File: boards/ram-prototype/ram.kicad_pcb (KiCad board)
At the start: 4 copper layers, 200 x 84 mm, 526 parts, among them J1 PinHeader_1x24_P2.54mm_Vertic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, J2 PinHeader_1x04_P2.54mm_Vertic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, J3 PinHeader_1x14_P2.54mm_Vertic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, U1 DSBGA\-5_NumericPads, U10 DSBGA\-5_NumericPads, U100 DSBGA\-5_NumericPads, U101 DSBGA\-5_NumericPads, U102 DSBGA\-5_NumericPads, U103 DSBGA\-5_NumericPads, U104 DSBGA\-5_NumericPads, U105 DSBGA\-5_NumericPads, U106 DSBGA\-5_NumericPads, U107 DSBGA\-5_NumericPads, U108 DSBGA\-5_NumericPads, U109 DSBGA\-5_NumericPads, U11 DSBGA\-5_NumericPads, U110 DSBGA\-5_NumericPads, U111 DSBGA\-5_NumericPads, U112 DSBGA\-5_NumericPads, U113 DSBGA\-5_NumericPads, U114 DSBGA\-5_NumericPads, U115 DSBGA\-5_NumericPads, U116 DSBGA\-5_NumericPads, U117 DSBGA\-5_NumericPads, U118 DSBGA\-5_NumericPads, U119 DSBGA\-5_NumericPads, U12 DSBGA\-5_NumericPads, U120 DSBGA\-5_NumericPads, U121 DSBGA\-5_NumericPads, U122 DSBGA\-5_NumericPads, U123 DSBGA\-5_NumericPads, U124 DSBGA\-5_NumericPads, U125 DSBGA\-5_NumericPads, U126 DSBGA\-5_NumericPads, U127 DSBGA\-5_NumericPads, U128 DSBGA\-5_NumericPads, U129 DSBGA\-5_NumericPads, U13 DSBGA\-5_NumericPads, U130 DSBGA\-5_NumericPads, U131 DSBGA\-5_NumericPads, U132 DSBGA\-5_NumericPads, U133 DSBGA\-5_NumericPads, U134 DSBGA\-5_NumericPads, U135 DSBGA\-5_NumericPads, U136 DSBGA\-5_NumericPads, U137 DSBGA\-5_NumericPads, U138 DSBGA\-5_NumericPads, U139 DSBGA\-5_NumericPads, U14 DSBGA\-5_NumericPads, U140 DSBGA\-5_NumericPads, U141 DSBGA\-5_NumericPads, U142 DSBGA\-5_NumericPads, U143 DSBGA\-5_NumericPads, U144 DSBGA\-5_NumericPads, U145 DSBGA\-5_NumericPads, U146 DSBGA\-5_NumericPads, U147 DSBGA\-5_NumericPads, U148 DSBGA\-5_NumericPads, U149 DSBGA\-5_NumericPads, U15 DSBGA\-5_NumericPads, U150 DSBGA\-5_NumericPads, U151 DSBGA\-5_NumericPads, U152 DSBGA\-5_NumericPads, U153 DSBGA\-5_NumericPads, U154 DSBGA\-5_NumericPads, U155 DSBGA\-5_NumericPads, U156 DSBGA\-5_NumericPads, U157 DSBGA\-5_NumericPads, U158 DSBGA\-5_NumericPads, U159 DSBGA\-5_NumericPads, U16 DSBGA\-5_NumericPads, U160 DSBGA\-5_NumericPads, U161 DSBGA\-5_NumericPads, U162 DSBGA\-5_NumericPads, U163 DSBGA\-5_NumericPads, U164 DSBGA\-5_NumericPads, U165 DSBGA\-5_NumericPads, U166 DSBGA\-5_NumericPads, U167 DSBGA\-5_NumericPads, U168 DSBGA\-5_NumericPads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

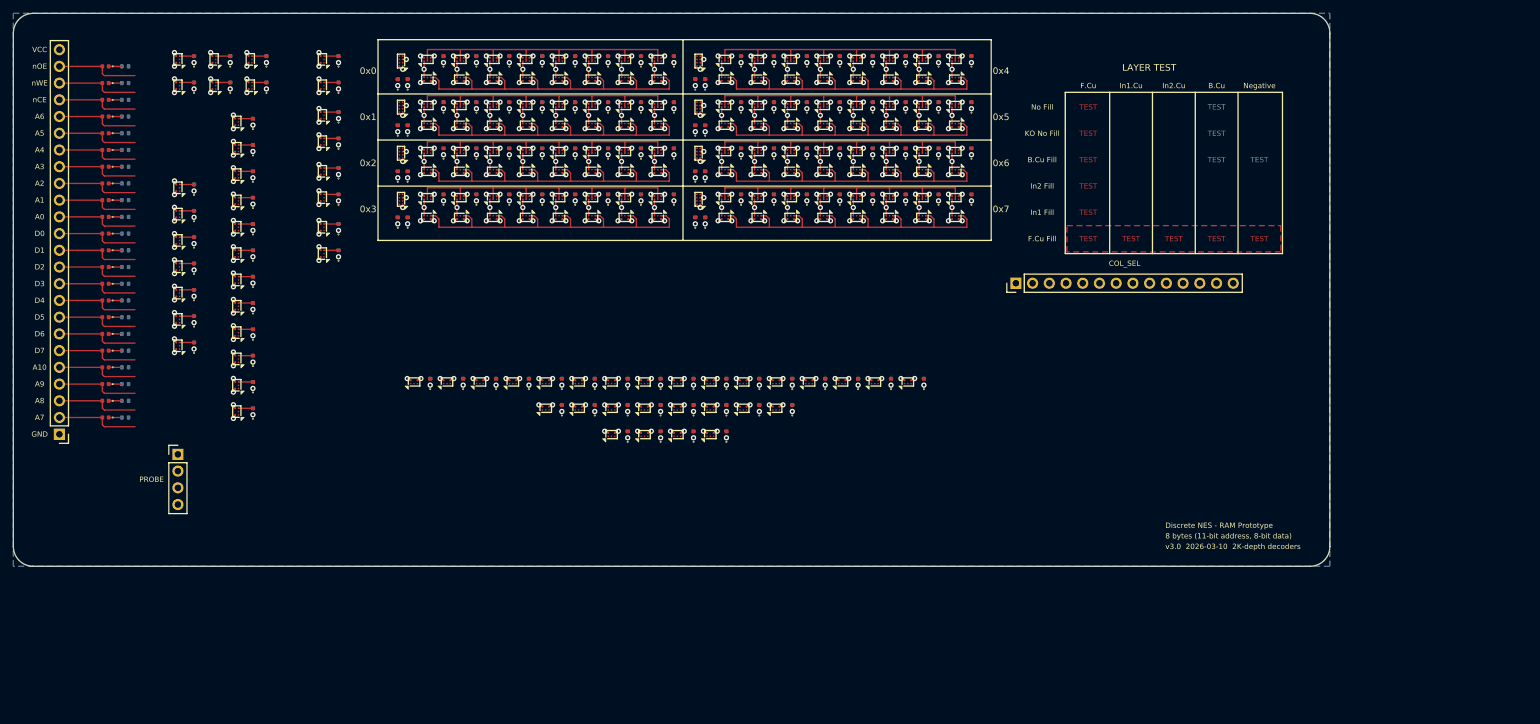
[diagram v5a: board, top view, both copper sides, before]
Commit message: Update row select to have the full complexity to test latency
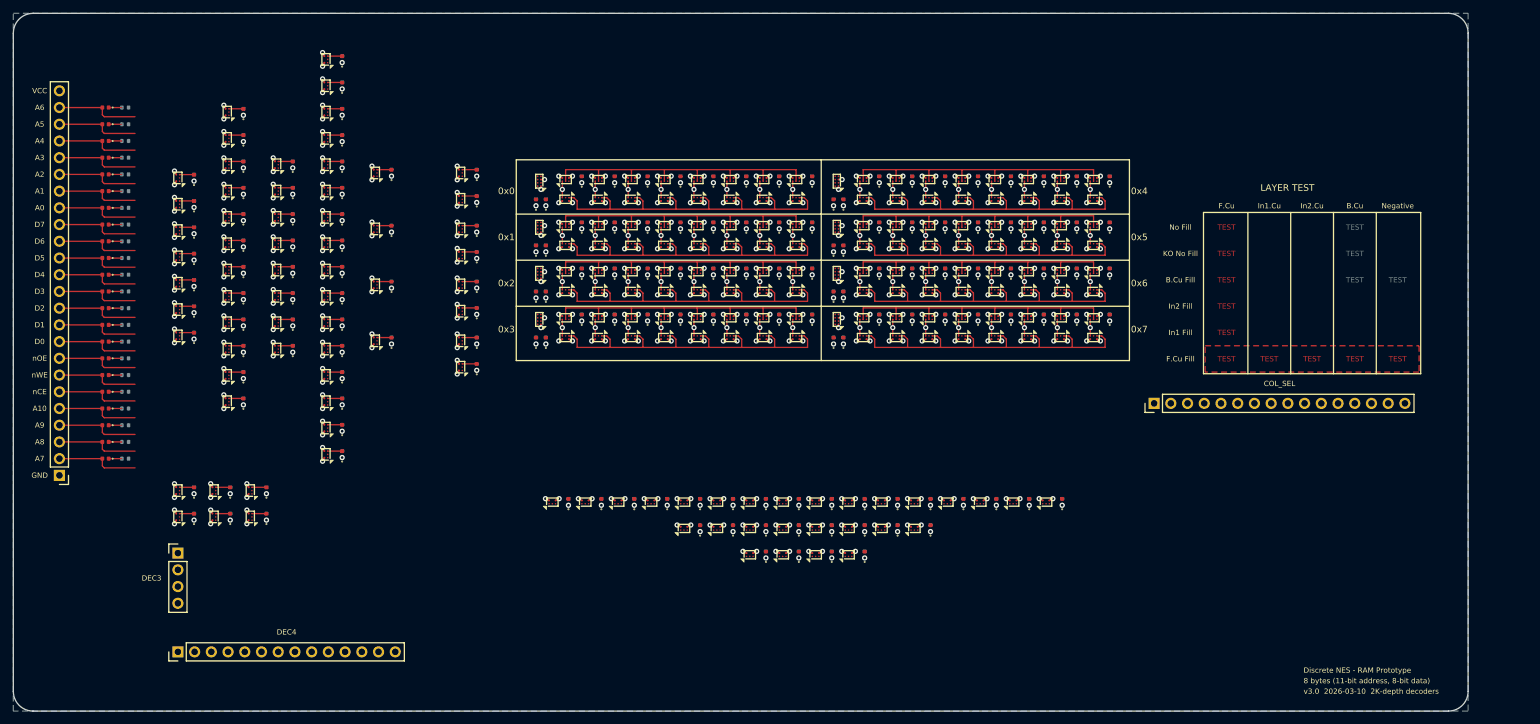
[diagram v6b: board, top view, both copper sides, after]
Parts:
- added D164: LED_0402_1005Metric, LED_SMD:LED_0402_1005Metric, F.Cu at (159.6, 38.2)
- added D165: LED_0402_1005Metric, LED_SMD:LED_0402_1005Metric, F.Cu at (159.6, 45.2)
- added D166: LED_0402_1005Metric, LED_SMD:LED_0402_1005Metric, F.Cu at (159.6, 52.2)
- added D167: LED_0402_1005Metric, LED_SMD:LED_0402_1005Metric, F.Cu at (159.6, 59.2)
- added D168: LED_0402_1005Metric, LED_SMD:LED_0402_1005Metric, F.Cu at (109.3, 38.2)
- added D169: LED_0402_1005Metric, LED_SMD:LED_0402_1005Metric, F.Cu at (109.3, 45.2)
- added D170: LED_0402_1005Metric, LED_SMD:LED_0402_1005Metric, F.Cu at (109.3, 52.2)
- added D171: LED_0402_1005Metric, LED_SMD:LED_0402_1005Metric, F.Cu at (109.3, 59.2)
- added D172: LED_0402_1005Metric, LED_SMD:LED_0402_1005Metric, F.Cu at (154.6, 38.2)
- added D173: LED_0402_1005Metric, LED_SMD:LED_0402_1005Metric, F.Cu at (154.6, 45.2)
- added D174: LED_0402_1005Metric, LED_SMD:LED_0402_1005Metric, F.Cu at (154.6, 52.2)
- added D175: LED_0402_1005Metric, LED_SMD:LED_0402_1005Metric, F.Cu at (154.6, 59.2)
- added D176: LED_0402_1005Metric, LED_SMD:LED_0402_1005Metric, F.Cu at (104.3, 38.2)
- added D177: LED_0402_1005Metric, LED_SMD:LED_0402_1005Metric, F.Cu at (104.3, 45.2)
- added D178: LED_0402_1005Metric, LED_SMD:LED_0402_1005Metric, F.Cu at (104.3, 52.2)
- added D179: LED_0402_1005Metric, LED_SMD:LED_0402_1005Metric, F.Cu at (104.3, 59.2)
- added D180: LED_0402_1005Metric, LED_SMD:LED_0402_1005Metric, F.Cu at (149.6, 38.2)
- added D181: LED_0402_1005Metric, LED_SMD:LED_0402_1005Metric, F.Cu at (149.6, 45.2)
- added D182: LED_0402_1005Metric, LED_SMD:LED_0402_1005Metric, F.Cu at (149.6, 52.2)
- added D183: LED_0402_1005Metric, LED_SMD:LED_0402_1005Metric, F.Cu at (149.6, 59.2)
- added D184: LED_0402_1005Metric, LED_SMD:LED_0402_1005Metric, F.Cu at (99.3, 38.2)
- added D185: LED_0402_1005Metric, LED_SMD:LED_0402_1005Metric, F.Cu at (99.3, 45.2)
- added D186: LED_0402_1005Metric, LED_SMD:LED_0402_1005Metric, F.Cu at (99.3, 52.2)
- added D187: LED_0402_1005Metric, LED_SMD:LED_0402_1005Metric, F.Cu at (99.3, 59.2)
- added D188: LED_0402_1005Metric, LED_SMD:LED_0402_1005Metric, F.Cu at (144.6, 38.2)
- added D189: LED_0402_1005Metric, LED_SMD:LED_0402_1005Metric, F.Cu at (144.6, 45.2)
- added D190: LED_0402_1005Metric, LED_SMD:LED_0402_1005Metric, F.Cu at (144.6, 52.2)
- added D191: LED_0402_1005Metric, LED_SMD:LED_0402_1005Metric, F.Cu at (144.6, 59.2)
- added J4: PinHeader_1x14_P2.54mm_Vertical, Connector_PinHeader_2.54mm:PinHeader_1x14_P2.54mm_Vertical, B.Cu at (38.0, 110.0)
- added R164: R_0402_1005Metric, Resistor_SMD:R_0402_1005Metric, B.Cu at (159.6, 38.2)
- added R165: R_0402_1005Metric, Resistor_SMD:R_0402_1005Metric, B.Cu at (159.6, 45.2)
- added R166: R_0402_1005Metric, Resistor_SMD:R_0402_1005Metric, B.Cu at (159.6, 52.2)
- added R167: R_0402_1005Metric, Resistor_SMD:R_0402_1005Metric, B.Cu at (159.6, 59.2)
- added R168: R_0402_1005Metric, Resistor_SMD:R_0402_1005Metric, B.Cu at (109.3, 38.2)
- added R169: R_0402_1005Metric, Resistor_SMD:R_0402_1005Metric, B.Cu at (109.3, 45.2)
- added R170: R_0402_1005Metric, Resistor_SMD:R_0402_1005Metric, B.Cu at (109.3, 52.2)
- added R171: R_0402_1005Metric, Resistor_SMD:R_0402_1005Metric, B.Cu at (109.3, 59.2)
- added R172: R_0402_1005Metric, Resistor_SMD:R_0402_1005Metric, B.Cu at (154.6, 38.2)
- added R173: R_0402_1005Metric, Resistor_SMD:R_0402_1005Metric, B.Cu at (154.6, 45.2)
- added R174: R_0402_1005Metric, Resistor_SMD:R_0402_1005Metric, B.Cu at (154.6, 52.2)
- added R175: R_0402_1005Metric, Resistor_SMD:R_0402_1005Metric, B.Cu at (154.6, 59.2)
- added R176: R_0402_1005Metric, Resistor_SMD:R_0402_1005Metric, B.Cu at (104.3, 38.2)
- added R177: R_0402_1005Metric, Resistor_SMD:R_0402_1005Metric, B.Cu at (104.3, 45.2)
- added R178: R_0402_1005Metric, Resistor_SMD:R_0402_1005Metric, B.Cu at (104.3, 52.2)
- added R179: R_0402_1005Metric, Resistor_SMD:R_0402_1005Metric, B.Cu at (104.3, 59.2)
- added R180: R_0402_1005Metric, Resistor_SMD:R_0402_1005Metric, B.Cu at (149.6, 38.2)
- added R181: R_0402_1005Metric, Resistor_SMD:R_0402_1005Metric, B.Cu at (149.6, 45.2)
- added R182: R_0402_1005Metric, Resistor_SMD:R_0402_1005Metric, B.Cu at (149.6, 52.2)
- added R183: R_0402_1005Metric, Resistor_SMD:R_0402_1005Metric, B.Cu at (149.6, 59.2)
- added R184: R_0402_1005Metric, Resistor_SMD:R_0402_1005Metric, B.Cu at (99.3, 38.2)
- added R185: R_0402_1005Metric, Resistor_SMD:R_0402_1005Metric, B.Cu at (99.3, 45.2)
- added R186: R_0402_1005Metric, Resistor_SMD:R_0402_1005Metric, B.Cu at (99.3, 52.2)
- added R187: R_0402_1005Metric, Resistor_SMD:R_0402_1005Metric, B.Cu at (99.3, 59.2)
- added R188: R_0402_1005Metric, Resistor_SMD:R_0402_1005Metric, B.Cu at (144.6, 38.2)
- added R189: R_0402_1005Metric, Resistor_SMD:R_0402_1005Metric, B.Cu at (144.6, 45.2)
- added R190: R_0402_1005Metric, Resistor_SMD:R_0402_1005Metric, B.Cu at (144.6, 52.2)
- added R191: R_0402_1005Metric, Resistor_SMD:R_0402_1005Metric, B.Cu at (144.6, 59.2)
- added U198: DSBGA\-5_NumericPads, DSBGA_Packages:DSBGA-5_NumericPads, F.Cu at (147.1, 38.2)
- added U199: DSBGA\-5_NumericPads, DSBGA_Packages:DSBGA-5_NumericPads, F.Cu at (147.1, 45.2)
- added U200: DSBGA\-5_NumericPads, DSBGA_Packages:DSBGA-5_NumericPads, F.Cu at (147.1, 52.2)
- added U201: DSBGA\-5_NumericPads, DSBGA_Packages:DSBGA-5_NumericPads, F.Cu at (147.1, 59.2)
- added U202: DSBGA\-5_NumericPads, DSBGA_Packages:DSBGA-5_NumericPads, F.Cu at (101.9, 41.2)
- added U203: DSBGA\-5_NumericPads, DSBGA_Packages:DSBGA-5_NumericPads, F.Cu at (101.9, 48.2)
- added U204: DSBGA\-5_NumericPads, DSBGA_Packages:DSBGA-5_NumericPads, F.Cu at (101.9, 55.2)
- added U205: DSBGA\-5_NumericPads, DSBGA_Packages:DSBGA-5_NumericPads, F.Cu at (101.9, 62.2)
- added U206: DSBGA\-5_NumericPads, DSBGA_Packages:DSBGA-5_NumericPads, F.Cu at (147.1, 41.2)
- added U207: DSBGA\-5_NumericPads, DSBGA_Packages:DSBGA-5_NumericPads, F.Cu at (147.1, 48.2)
- added U208: DSBGA\-5_NumericPads, DSBGA_Packages:DSBGA-5_NumericPads, F.Cu at (147.1, 55.2)
- added U209: DSBGA\-5_NumericPads, DSBGA_Packages:DSBGA-5_NumericPads, F.Cu at (147.1, 62.2)
- added U210: DSBGA\-5_NumericPads, DSBGA_Packages:DSBGA-5_NumericPads, F.Cu at (96.9, 38.2)
- added U211: DSBGA\-5_NumericPads, DSBGA_Packages:DSBGA-5_NumericPads, F.Cu at (96.9, 45.2)
- added U212: DSBGA\-5_NumericPads, DSBGA_Packages:DSBGA-5_NumericPads, F.Cu at (96.9, 52.2)
- added U213: DSBGA\-5_NumericPads, DSBGA_Packages:DSBGA-5_NumericPads, F.Cu at (96.9, 59.2)
- added U214: DSBGA\-5_NumericPads, DSBGA_Packages:DSBGA-5_NumericPads, F.Cu at (142.1, 38.2)
- added U215: DSBGA\-5_NumericPads, DSBGA_Packages:DSBGA-5_NumericPads, F.Cu at (142.1, 45.2)
- added U216: DSBGA\-5_NumericPads, DSBGA_Packages:DSBGA-5_NumericPads, F.Cu at (142.1, 52.2)
- added U217: DSBGA\-5_NumericPads, DSBGA_Packages:DSBGA-5_NumericPads, F.Cu at (142.1, 59.2)
- added U218: DSBGA\-5_NumericPads, DSBGA_Packages:DSBGA-5_NumericPads, F.Cu at (96.9, 41.2)
- added U219: DSBGA\-5_NumericPads, DSBGA_Packages:DSBGA-5_NumericPads, F.Cu at (96.9, 48.2)
- added U220: DSBGA\-5_NumericPads, DSBGA_Packages:DSBGA-5_NumericPads, F.Cu at (96.9, 55.2)
- added U221: DSBGA\-5_NumericPads, DSBGA_Packages:DSBGA-5_NumericPads, F.Cu at (96.9, 62.2)
- added U222: DSBGA\-5_NumericPads, DSBGA_Packages:DSBGA-5_NumericPads, F.Cu at (142.1, 41.2)
- added U223: DSBGA\-5_NumericPads, DSBGA_Packages:DSBGA-5_NumericPads, F.Cu at (142.1, 48.2)
- added U224: DSBGA\-5_NumericPads, DSBGA_Packages:DSBGA-5_NumericPads, F.Cu at (142.1, 55.2)
- added U225: DSBGA\-5_NumericPads, DSBGA_Packages:DSBGA-5_NumericPads, F.Cu at (142.1, 62.2)
- J3: value PinHeader_1x14_P2.54mm_Vertical -> PinHeader_1x16_P2.54mm_Vertical; footprint Connector_PinHeader_2.54mm:PinHeader_1x14_P2.54mm_Vertical -> Connector_PinHeader_2.54mm:PinHeader_1x16_P2.54mm_Vertical
- U62, U63, U64, U65, U66, U67, U68, U69: value DSBGA\-8_NumericPads -> DSBGA\-5_NumericPads; footprint DSBGA_Packages:DSBGA-8_NumericPads -> DSBGA_Packages:DSBGA-5_NumericPads
- U90, U91, U92, U93, U94, U95, U96, U97: value DSBGA\-5_NumericPads -> DSBGA\-8_NumericPads; footprint DSBGA_Packages:DSBGA-5_NumericPads -> DSBGA_Packages:DSBGA-8_NumericPads
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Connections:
- D1 pad 2: /Control Logic/nOE -> /Address Decoder/A6
- D10 pad 2: /Address Decoder/A0 -> /D5
- D100 pad 2: Net-(D100-A) -> /WRITE_EN_ROW_2
- D101 pad 2: Net-(D101-A) -> /WRITE_EN_ROW_3
- D102 pad 2: Net-(D102-A) -> /READ_EN_ROW_0
- D103 pad 2: Net-(D103-A) -> /READ_EN_ROW_1
- D104 pad 2: Net-(D104-A) -> /READ_EN_ROW_2
- D105 pad 2: Net-(D105-A) -> /READ_EN_ROW_3
- D11 pad 2: /D0 -> /D4
- D110 pad 2: Net-(D110-A) -> /WRITE_ACTIVE
- D111 pad 2: Net-(D111-A) -> /READ_EN
- D12 pad 2: /D1 -> /D3
- D14 pad 2: /D3 -> /D1
- D15 pad 2: /D4 -> /D0
- D16 pad 2: /D5 -> /nOE
- D17 pad 2: /D6 -> /nWE
- D18 pad 2: /D7 -> /nCE
- D2 pad 2: /Control Logic/nWE -> /Address Decoder/A5
- D23 pad 2: Net-(D23-A) -> /Address Decoder/nA0
- D24 pad 2: Net-(D24-A) -> /Address Decoder/nA1
- D25 pad 2: Net-(D25-A) -> /Address Decoder/nA2
- D26 pad 2: Net-(D26-A) -> /Address Decoder/nA3
- D27 pad 2: Net-(D27-A) -> /Address Decoder/nA4
- D28 pad 2: Net-(D28-A) -> /Address Decoder/nA5
- D29 pad 2: Net-(D29-A) -> /Address Decoder/nA6
- D3 pad 2: /Control Logic/nCE -> /Address Decoder/A4
- D30 pad 2: /RS1 -> /Address Decoder/G0
- D31 pad 2: /RS2 -> /Address Decoder/G1
- D32 pad 2: /RS3 -> /Address Decoder/G2
- D33 pad 2: /RS4 -> /Address Decoder/G3
- D34 pad 2: Net-(D34-A) -> /Address Decoder/DEC3_0
- D35 pad 2: Net-(D35-A) -> /Address Decoder/DEC3_1
- D36 pad 2: Net-(D36-A) -> /Address Decoder/DEC3_2
- D37 pad 2: Net-(D37-A) -> /Address Decoder/DEC3_3
- D38 pad 2: /Address Decoder/ROW_SEL_0 -> /DEC3_4
- D39 pad 2: /Address Decoder/ROW_SEL_1 -> /DEC3_5
- D4 pad 2: /Address Decoder/A6 -> /Address Decoder/A3
- D40 pad 2: /Address Decoder/ROW_SEL_2 -> /DEC3_6
- D41 pad 2: /Address Decoder/ROW_SEL_3 -> /DEC3_7
- D42 pad 2: Net-(D42-A) -> /Address Decoder/HA0
- D43 pad 2: Net-(D43-A) -> /Address Decoder/HA1
- D44 pad 2: Net-(D44-A) -> /Address Decoder/HA2
- D45 pad 2: Net-(D45-A) -> /Address Decoder/HA3
- D46 pad 2: /Column Select/GA0 -> /Address Decoder/HB0
- D47 pad 2: /Column Select/GA1 -> /Address Decoder/HB1
- D48 pad 2: /Column Select/GA2 -> /Address Decoder/HB2
- D49 pad 2: /Column Select/GA3 -> /Address Decoder/HB3
- D5 pad 2: /Address Decoder/A5 -> /Address Decoder/A2
- D50 pad 2: /Column Select/GB0 -> /Address Decoder/DEC4_0
- D51 pad 2: /Column Select/GB1 -> /DEC4_1
- D52 pad 2: /Column Select/GB2 -> /DEC4_2
- D53 pad 2: /Column Select/GB3 -> /DEC4_3
- D54 pad 2: /COL_SEL_0 -> /DEC4_4
- D55 pad 2: /COL_SEL_1 -> /DEC4_5
- D56 pad 2: /COL_SEL_2 -> /DEC4_6
- D57 pad 2: /COL_SEL_3 -> /DEC4_7
- D58 pad 2: /COL_SEL_4 -> /DEC4_8
- D59 pad 2: /COL_SEL_5 -> /DEC4_9
- D6 pad 2: /Address Decoder/A4 -> /Address Decoder/A1
- D60 pad 2: /COL_SEL_6 -> /DEC4_10
- D61 pad 2: /COL_SEL_7 -> /DEC4_11
- D62 pad 2: /COL_SEL_8 -> /DEC4_12
- D63 pad 2: /COL_SEL_9 -> /DEC4_13
- D64 pad 2: /COL_SEL_10 -> /DEC4_14
- D65 pad 2: /COL_SEL_11 -> /DEC4_15
- D66 pad 2: /COL_SEL_12 -> /Address Decoder/ROW_SEL_0
- D67 pad 2: /COL_SEL_13 -> /Address Decoder/ROW_SEL_1
- D68 pad 2: /COL_SEL_14 -> /Address Decoder/ROW_SEL_2
- D69 pad 2: /COL_SEL_15 -> /Address Decoder/ROW_SEL_3
- D7 pad 2: /Address Decoder/A3 -> /Address Decoder/A0
- D74 pad 2: /WRITE_ACTIVE -> /Column Select/GA0
- D75 pad 2: /READ_EN -> /Column Select/GA1
- D76 pad 2: /WRITE_EN_ROW_0 -> /Column Select/GA2
- D77 pad 2: /WRITE_EN_ROW_1 -> /Column Select/GA3
- D78 pad 2: /WRITE_EN_ROW_2 -> /Column Select/GB0
- D79 pad 2: /WRITE_EN_ROW_3 -> /Column Select/GB1
- D8 pad 2: /Address Decoder/A2 -> /D7
- D80 pad 2: /READ_EN_ROW_0 -> /Column Select/GB2
- D81 pad 2: /READ_EN_ROW_1 -> /Column Select/GB3
- D82 pad 2: /READ_EN_ROW_2 -> /COL_SEL_0
- D83 pad 2: /READ_EN_ROW_3 -> /COL_SEL_1
- D84 pad 2: Net-(D84-A) -> /COL_SEL_2
- D85 pad 2: Net-(D85-A) -> /COL_SEL_3
- D86 pad 2: Net-(D86-A) -> /COL_SEL_4
- D87 pad 2: Net-(D87-A) -> /COL_SEL_5
- D88 pad 2: Net-(D88-A) -> /COL_SEL_6
- D89 pad 2: Net-(D89-A) -> /COL_SEL_7
- D9 pad 2: /Address Decoder/A1 -> /D6
- D90 pad 2: Net-(D90-A) -> /COL_SEL_8
- D91 pad 2: Net-(D91-A) -> /COL_SEL_9
- D92 pad 2: Net-(D92-A) -> /COL_SEL_10
- D93 pad 2: Net-(D93-A) -> /COL_SEL_11
- D94 pad 2: Net-(D94-A) -> /COL_SEL_12
- D95 pad 2: Net-(D95-A) -> /COL_SEL_13
- D96 pad 2: Net-(D96-A) -> /COL_SEL_14
- D97 pad 2: Net-(D97-A) -> /COL_SEL_15
- D98 pad 2: Net-(D98-A) -> /WRITE_EN_ROW_0
- D99 pad 2: Net-(D99-A) -> /WRITE_EN_ROW_1
- J1 pad 10: /D3 -> /D1
- J1 pad 12: /D1 -> /D3
- J1 pad 13: /D0 -> /D4
- J1 pad 14: /Address Decoder/A0 -> /D5
- J1 pad 15: /Address Decoder/A1 -> /D6
- J1 pad 16: /Address Decoder/A2 -> /D7
- J1 pad 17: /Address Decoder/A3 -> /Address Decoder/A0
- J1 pad 18: /Address Decoder/A4 -> /Address Decoder/A1
- J1 pad 19: /Address Decoder/A5 -> /Address Decoder/A2
- J1 pad 20: /Address Decoder/A6 -> /Address Decoder/A3
- J1 pad 21: /Control Logic/nCE -> /Address Decoder/A4
- J1 pad 22: /Control Logic/nWE -> /Address Decoder/A5
- J1 pad 23: /Control Logic/nOE -> /Address Decoder/A6
- J1 pad 6: /D7 -> /nCE
- J1 pad 7: /D6 -> /nWE
- J1 pad 8: /D5 -> /nOE
- J1 pad 9: /D4 -> /D0
- J2 pad 1: /RS1 -> /DEC3_4
- J2 pad 2: /RS2 -> /DEC3_5
- J2 pad 3: /RS3 -> /DEC3_6
- J2 pad 4: /RS4 -> /DEC3_7
- J3 pad 1: /COL_SEL_2 -> /DEC4_1
- J3 pad 10: /COL_SEL_11 -> /DEC4_10
- J3 pad 11: /COL_SEL_12 -> /DEC4_11
- J3 pad 12: /COL_SEL_13 -> /DEC4_12
- J3 pad 13: /COL_SEL_14 -> /DEC4_13
- J3 pad 14: /COL_SEL_15 -> /DEC4_14
- J3 pad 2: /COL_SEL_3 -> /DEC4_2
- J3 pad 3: /COL_SEL_4 -> /DEC4_3
- J3 pad 4: /COL_SEL_5 -> /DEC4_4
- J3 pad 5: /COL_SEL_6 -> /DEC4_5
- J3 pad 6: /COL_SEL_7 -> /DEC4_6
- J3 pad 7: /COL_SEL_8 -> /DEC4_7
- J3 pad 8: /COL_SEL_9 -> /DEC4_8
- J3 pad 9: /COL_SEL_10 -> /DEC4_9
- U1 pad 4: Net-(D23-A) -> /Address Decoder/nA0
- U10 pad 1: /RS1 -> /Address Decoder/A2
- U10 pad 2: /RS2 -> /Address Decoder/nA1
- U10 pad 4: /RS3 -> /Address Decoder/G2
- U100 pad 1: Net-(D98-A) -> /D0
- U100 pad 4: /D1 -> Net-(D130-A)
- U101 pad 1: Net-(D99-A) -> /D0
- U101 pad 4: /D1 -> Net-(D131-A)
- U102 pad 1: /D2 -> /D0
- U102 pad 2: Net-(D84-A) -> Net-(D116-A)
- U102 pad 4: Net-(D116-A) -> Net-(D132-A)
- U103 pad 1: /D2 -> /D0
- U103 pad 2: Net-(D85-A) -> Net-(D117-A)
- U103 pad 4: Net-(D117-A) -> Net-(D133-A)
- U104 pad 1: /D2 -> /D0
- U104 pad 2: Net-(D86-A) -> Net-(D118-A)
- U104 pad 4: Net-(D118-A) -> Net-(D134-A)
- U105 pad 1: /D2 -> /D0
- U105 pad 2: Net-(D87-A) -> Net-(D119-A)
- U105 pad 4: Net-(D119-A) -> Net-(D135-A)
- U106 pad 1: /D2 -> Net-(D120-A)
- U106 pad 2: Net-(D88-A) -> Net-(D128-A)
- U106 pad 4: Net-(D120-A) -> /D0
- U107 pad 1: /D2 -> Net-(D121-A)
- U107 pad 2: Net-(D89-A) -> Net-(D129-A)
- U107 pad 4: Net-(D121-A) -> /D0
- U108 pad 1: /D2 -> Net-(D122-A)
- U108 pad 2: Net-(D90-A) -> Net-(D130-A)
- U108 pad 4: Net-(D122-A) -> /D0
- U109 pad 1: /D2 -> Net-(D123-A)
- U109 pad 2: Net-(D91-A) -> Net-(D131-A)
- U109 pad 4: Net-(D123-A) -> /D0
- U11 pad 1: /RS3 -> /Address Decoder/A2
- U11 pad 2: Net-(D29-A) -> /Address Decoder/A1
- U11 pad 4: /RS4 -> /Address Decoder/G3
- U110 pad 1: Net-(D92-A) -> Net-(D124-A)
- U110 pad 2: Net-(D116-A) -> Net-(D132-A)
- U110 pad 4: /D2 -> /D0
- U111 pad 1: Net-(D93-A) -> Net-(D125-A)
- U111 pad 2: Net-(D117-A) -> Net-(D133-A)
- U111 pad 4: /D2 -> /D0
- U112 pad 1: Net-(D94-A) -> Net-(D126-A)
- U112 pad 2: Net-(D118-A) -> Net-(D134-A)
- U112 pad 4: /D2 -> /D0
- U113 pad 1: Net-(D95-A) -> Net-(D127-A)
- U113 pad 2: Net-(D119-A) -> Net-(D135-A)
- U113 pad 4: /D2 -> /D0
- U114 pad 1: Net-(D96-A) -> /D1
- U114 pad 2: Net-(D120-A) -> Net-(D112-A)
- U114 pad 4: /D2 -> Net-(D136-A)
- U115 pad 1: Net-(D97-A) -> /D1
- U115 pad 2: Net-(D121-A) -> Net-(D113-A)
- U115 pad 4: /D2 -> Net-(D137-A)
- U116 pad 1: Net-(D98-A) -> /D1
- U116 pad 2: Net-(D122-A) -> Net-(D114-A)
- U116 pad 4: /D2 -> Net-(D138-A)
- U117 pad 1: Net-(D99-A) -> /D1
- U117 pad 2: Net-(D123-A) -> Net-(D115-A)
- U117 pad 4: /D2 -> Net-(D139-A)
- U118 pad 1: /D3 -> /D1
- U118 pad 2: Net-(D84-A) -> Net-(D116-A)
- U118 pad 4: Net-(D124-A) -> Net-(D140-A)
- U119 pad 1: /D3 -> /D1
- U119 pad 2: Net-(D85-A) -> Net-(D117-A)
- U119 pad 4: Net-(D125-A) -> Net-(D141-A)
- U12 pad 1: Net-(D24-A) -> /Address Decoder/G0
- U12 pad 2: Net-(D23-A) -> /Address Decoder/nA0
- U12 pad 4: Net-(D34-A) -> /Address Decoder/DEC3_0
- U120 pad 1: /D3 -> /D1
- U120 pad 2: Net-(D86-A) -> Net-(D118-A)
- U120 pad 4: Net-(D126-A) -> Net-(D142-A)
- U121 pad 1: /D3 -> /D1
- U121 pad 2: Net-(D87-A) -> Net-(D119-A)
- U121 pad 4: Net-(D127-A) -> Net-(D143-A)
- U122 pad 1: /D3 -> Net-(D120-A)
- U122 pad 2: Net-(D88-A) -> Net-(D136-A)
- U122 pad 4: Net-(D128-A) -> /D1
- U123 pad 1: /D3 -> Net-(D121-A)
- U123 pad 2: Net-(D89-A) -> Net-(D137-A)
- U123 pad 4: Net-(D129-A) -> /D1
- U124 pad 1: /D3 -> Net-(D122-A)
- U124 pad 2: Net-(D90-A) -> Net-(D138-A)
- U124 pad 4: Net-(D130-A) -> /D1
- U125 pad 1: /D3 -> Net-(D123-A)
- U125 pad 2: Net-(D91-A) -> Net-(D139-A)
- U125 pad 4: Net-(D131-A) -> /D1
- U126 pad 1: Net-(D92-A) -> Net-(D124-A)
- U126 pad 2: Net-(D124-A) -> Net-(D140-A)
- U126 pad 4: /D3 -> /D1
- U127 pad 1: Net-(D93-A) -> Net-(D125-A)
- U127 pad 2: Net-(D125-A) -> Net-(D141-A)
- U127 pad 4: /D3 -> /D1
- U128 pad 1: Net-(D94-A) -> Net-(D126-A)
- U128 pad 2: Net-(D126-A) -> Net-(D142-A)
- U128 pad 4: /D3 -> /D1
- U129 pad 1: Net-(D95-A) -> Net-(D127-A)
- U129 pad 2: Net-(D127-A) -> Net-(D143-A)
- U129 pad 4: /D3 -> /D1
- U13 pad 1: Net-(D24-A) -> /Address Decoder/G0
- U13 pad 4: Net-(D35-A) -> /Address Decoder/DEC3_1
- U130 pad 1: Net-(D96-A) -> /D2
- U130 pad 2: Net-(D128-A) -> Net-(D112-A)
- U130 pad 4: /D3 -> Net-(D144-A)
- U131 pad 1: Net-(D97-A) -> /D2
- U131 pad 2: Net-(D129-A) -> Net-(D113-A)
- U131 pad 4: /D3 -> Net-(D145-A)
- U132 pad 1: Net-(D98-A) -> /D2
- U132 pad 2: Net-(D130-A) -> Net-(D114-A)
- U132 pad 4: /D3 -> Net-(D146-A)
- U133 pad 1: Net-(D99-A) -> /D2
- U133 pad 2: Net-(D131-A) -> Net-(D115-A)
- U133 pad 4: /D3 -> Net-(D147-A)
- U134 pad 1: /D4 -> /D2
- U134 pad 2: Net-(D84-A) -> Net-(D116-A)
- U134 pad 4: Net-(D132-A) -> Net-(D148-A)
- U135 pad 1: /D4 -> /D2
- U135 pad 2: Net-(D85-A) -> Net-(D117-A)
- U135 pad 4: Net-(D133-A) -> Net-(D149-A)
- U136 pad 1: /D4 -> /D2
- U136 pad 2: Net-(D86-A) -> Net-(D118-A)
- U136 pad 4: Net-(D134-A) -> Net-(D150-A)
- U137 pad 1: /D4 -> /D2
- U137 pad 2: Net-(D87-A) -> Net-(D119-A)
- U137 pad 4: Net-(D135-A) -> Net-(D151-A)
- U138 pad 1: /D4 -> Net-(D120-A)
- U138 pad 2: Net-(D88-A) -> Net-(D144-A)
- U138 pad 4: Net-(D136-A) -> /D2
- U139 pad 1: /D4 -> Net-(D121-A)
- U139 pad 2: Net-(D89-A) -> Net-(D145-A)
- U139 pad 4: Net-(D137-A) -> /D2
- U14 pad 1: /Address Decoder/A1 -> /Address Decoder/G1
- U14 pad 2: Net-(D23-A) -> /Address Decoder/nA0
- U14 pad 4: Net-(D36-A) -> /Address Decoder/DEC3_2
- U140 pad 1: /D4 -> Net-(D122-A)
- U140 pad 2: Net-(D90-A) -> Net-(D146-A)
- U140 pad 4: Net-(D138-A) -> /D2
- U141 pad 1: /D4 -> Net-(D123-A)
- U141 pad 2: Net-(D91-A) -> Net-(D147-A)
- U141 pad 4: Net-(D139-A) -> /D2
- U142 pad 1: Net-(D92-A) -> Net-(D124-A)
- U142 pad 2: Net-(D132-A) -> Net-(D148-A)
- U142 pad 4: /D4 -> /D2
- U143 pad 1: Net-(D93-A) -> Net-(D125-A)
- U143 pad 2: Net-(D133-A) -> Net-(D149-A)
- U143 pad 4: /D4 -> /D2
- U144 pad 1: Net-(D94-A) -> Net-(D126-A)
- U144 pad 2: Net-(D134-A) -> Net-(D150-A)
- U144 pad 4: /D4 -> /D2
- U145 pad 1: Net-(D95-A) -> Net-(D127-A)
- U145 pad 2: Net-(D135-A) -> Net-(D151-A)
- U145 pad 4: /D4 -> /D2
- U146 pad 1: Net-(D96-A) -> /D3
- U146 pad 2: Net-(D136-A) -> Net-(D112-A)
- U146 pad 4: /D4 -> Net-(D152-A)
- U147 pad 1: Net-(D97-A) -> /D3
- U147 pad 2: Net-(D137-A) -> Net-(D113-A)
- U147 pad 4: /D4 -> Net-(D153-A)
- U148 pad 1: Net-(D98-A) -> /D3
- U148 pad 2: Net-(D138-A) -> Net-(D114-A)
- U148 pad 4: /D4 -> Net-(D154-A)
- U149 pad 1: Net-(D99-A) -> /D3
- U149 pad 2: Net-(D139-A) -> Net-(D115-A)
- U149 pad 4: /D4 -> Net-(D155-A)
- U15 pad 1: /Address Decoder/A1 -> /Address Decoder/G1
- U15 pad 4: Net-(D37-A) -> /Address Decoder/DEC3_3
- U150 pad 1: /D5 -> /D3
- U150 pad 2: Net-(D84-A) -> Net-(D116-A)
- U150 pad 4: Net-(D140-A) -> Net-(D156-A)
- U151 pad 1: /D5 -> /D3
- U151 pad 2: Net-(D85-A) -> Net-(D117-A)
- U151 pad 4: Net-(D141-A) -> Net-(D157-A)
- U152 pad 1: /D5 -> /D3
- U152 pad 2: Net-(D86-A) -> Net-(D118-A)
- U152 pad 4: Net-(D142-A) -> Net-(D158-A)
- U153 pad 1: /D5 -> /D3
- U153 pad 2: Net-(D87-A) -> Net-(D119-A)
- U153 pad 4: Net-(D143-A) -> Net-(D159-A)
- U154 pad 1: /D5 -> Net-(D120-A)
- U154 pad 2: Net-(D88-A) -> Net-(D152-A)
- U154 pad 4: Net-(D144-A) -> /D3
- U155 pad 1: /D5 -> Net-(D121-A)
- U155 pad 2: Net-(D89-A) -> Net-(D153-A)
- U155 pad 4: Net-(D145-A) -> /D3
- U156 pad 1: /D5 -> Net-(D122-A)
- U156 pad 2: Net-(D90-A) -> Net-(D154-A)
- U156 pad 4: Net-(D146-A) -> /D3
- U157 pad 1: /D5 -> Net-(D123-A)
- U157 pad 2: Net-(D91-A) -> Net-(D155-A)
- U157 pad 4: Net-(D147-A) -> /D3
- U158 pad 1: Net-(D92-A) -> Net-(D124-A)
- U158 pad 2: Net-(D140-A) -> Net-(D156-A)
- U158 pad 4: /D5 -> /D3
- U159 pad 1: Net-(D93-A) -> Net-(D125-A)
- U159 pad 2: Net-(D141-A) -> Net-(D157-A)
- U159 pad 4: /D5 -> /D3
- U16 pad 1: /RS4 -> /Address Decoder/G2
- U16 pad 2: Net-(D34-A) -> /Address Decoder/nA0
- U16 pad 4: /Address Decoder/ROW_SEL_0 -> /DEC3_4
- U160 pad 1: Net-(D94-A) -> Net-(D126-A)
- U160 pad 2: Net-(D142-A) -> Net-(D158-A)
- U160 pad 4: /D5 -> /D3
- U161 pad 1: Net-(D95-A) -> Net-(D127-A)
- U161 pad 2: Net-(D143-A) -> Net-(D159-A)
- U161 pad 4: /D5 -> /D3
- U162 pad 1: Net-(D96-A) -> /D4
- U162 pad 2: Net-(D144-A) -> Net-(D112-A)
- U162 pad 4: /D5 -> Net-(D160-A)
- U163 pad 1: Net-(D97-A) -> /D4
- U163 pad 2: Net-(D145-A) -> Net-(D113-A)
- U163 pad 4: /D5 -> Net-(D161-A)
- U164 pad 1: Net-(D98-A) -> /D4
- U164 pad 2: Net-(D146-A) -> Net-(D114-A)
- U164 pad 4: /D5 -> Net-(D162-A)
- U165 pad 1: Net-(D99-A) -> /D4
- U165 pad 2: Net-(D147-A) -> Net-(D115-A)
- U165 pad 4: /D5 -> Net-(D163-A)
- U166 pad 1: /D6 -> /D4
- U166 pad 2: Net-(D84-A) -> Net-(D116-A)
- U166 pad 4: Net-(D148-A) -> Net-(D164-A)
- U167 pad 1: /D6 -> /D4
- U167 pad 2: Net-(D85-A) -> Net-(D117-A)
- U167 pad 4: Net-(D149-A) -> Net-(D165-A)
- U168 pad 1: /D6 -> /D4
- U168 pad 2: Net-(D86-A) -> Net-(D118-A)
- U168 pad 4: Net-(D150-A) -> Net-(D166-A)
- U169 pad 1: /D6 -> /D4
- U169 pad 2: Net-(D87-A) -> Net-(D119-A)
- U169 pad 4: Net-(D151-A) -> Net-(D167-A)
- U17 pad 1: /RS4 -> /Address Decoder/G2
- U17 pad 2: Net-(D35-A) -> /Address Decoder/A0
- U17 pad 4: /Address Decoder/ROW_SEL_1 -> /DEC3_5
- U170 pad 1: /D6 -> Net-(D120-A)
- U170 pad 2: Net-(D88-A) -> Net-(D160-A)
- U170 pad 4: Net-(D152-A) -> /D4
- U171 pad 1: /D6 -> Net-(D121-A)
- U171 pad 2: Net-(D89-A) -> Net-(D161-A)
- U171 pad 4: Net-(D153-A) -> /D4
- U172 pad 1: /D6 -> Net-(D122-A)
- U172 pad 2: Net-(D90-A) -> Net-(D162-A)
- U172 pad 4: Net-(D154-A) -> /D4
- U173 pad 1: /D6 -> Net-(D123-A)
- U173 pad 2: Net-(D91-A) -> Net-(D163-A)
- U173 pad 4: Net-(D155-A) -> /D4
- U174 pad 1: Net-(D92-A) -> Net-(D124-A)
- U174 pad 2: Net-(D148-A) -> Net-(D164-A)
- U174 pad 4: /D6 -> /D4
- U175 pad 1: Net-(D93-A) -> Net-(D125-A)
- U175 pad 2: Net-(D149-A) -> Net-(D165-A)
- U175 pad 4: /D6 -> /D4
- U176 pad 1: Net-(D94-A) -> Net-(D126-A)
- U176 pad 2: Net-(D150-A) -> Net-(D166-A)
- U176 pad 4: /D6 -> /D4
- U177 pad 1: Net-(D95-A) -> Net-(D127-A)
- U177 pad 2: Net-(D151-A) -> Net-(D167-A)
- U177 pad 4: /D6 -> /D4
- U178 pad 1: Net-(D96-A) -> /D5
- U178 pad 2: Net-(D152-A) -> Net-(D112-A)
- U178 pad 4: /D6 -> Net-(D168-A)
- U179 pad 1: Net-(D97-A) -> /D5
- U179 pad 2: Net-(D153-A) -> Net-(D113-A)
- U179 pad 4: /D6 -> Net-(D169-A)
- U18 pad 1: /RS4 -> /Address Decoder/G3
- U18 pad 2: Net-(D36-A) -> /Address Decoder/nA0
- U18 pad 4: /Address Decoder/ROW_SEL_2 -> /DEC3_6
- U180 pad 1: Net-(D98-A) -> /D5
- U180 pad 2: Net-(D154-A) -> Net-(D114-A)
- U180 pad 4: /D6 -> Net-(D170-A)
- U181 pad 1: Net-(D99-A) -> /D5
- U181 pad 2: Net-(D155-A) -> Net-(D115-A)
- U181 pad 4: /D6 -> Net-(D171-A)
- U182 pad 1: /D7 -> /D5
- U182 pad 2: Net-(D84-A) -> Net-(D116-A)
- U182 pad 4: Net-(D156-A) -> Net-(D172-A)
- U183 pad 1: /D7 -> /D5
- U183 pad 2: Net-(D85-A) -> Net-(D117-A)
- U183 pad 4: Net-(D157-A) -> Net-(D173-A)
- U184 pad 1: /D7 -> /D5
- U184 pad 2: Net-(D86-A) -> Net-(D118-A)
- U184 pad 4: Net-(D158-A) -> Net-(D174-A)
- U185 pad 1: /D7 -> /D5
- U185 pad 2: Net-(D87-A) -> Net-(D119-A)
- U185 pad 4: Net-(D159-A) -> Net-(D175-A)
- U186 pad 1: /D7 -> Net-(D120-A)
- U186 pad 2: Net-(D88-A) -> Net-(D168-A)
- U186 pad 4: Net-(D160-A) -> /D5
- U187 pad 1: /D7 -> Net-(D121-A)
- U187 pad 2: Net-(D89-A) -> Net-(D169-A)
- U187 pad 4: Net-(D161-A) -> /D5
- U188 pad 1: /D7 -> Net-(D122-A)
- U188 pad 2: Net-(D90-A) -> Net-(D170-A)
- U188 pad 4: Net-(D162-A) -> /D5
- U189 pad 1: /D7 -> Net-(D123-A)
- U189 pad 2: Net-(D91-A) -> Net-(D171-A)
- U189 pad 4: Net-(D163-A) -> /D5
- U19 pad 1: /RS4 -> /Address Decoder/G3
- U19 pad 2: Net-(D37-A) -> /Address Decoder/A0
- U19 pad 4: /Address Decoder/ROW_SEL_3 -> /DEC3_7
- U190 pad 1: Net-(D92-A) -> Net-(D124-A)
- U190 pad 2: Net-(D156-A) -> Net-(D172-A)
- U190 pad 4: /D7 -> /D5
- U191 pad 1: Net-(D93-A) -> Net-(D125-A)
- U191 pad 2: Net-(D157-A) -> Net-(D173-A)
- U191 pad 4: /D7 -> /D5
- U192 pad 1: Net-(D94-A) -> Net-(D126-A)
- U192 pad 2: Net-(D158-A) -> Net-(D174-A)
- U192 pad 4: /D7 -> /D5
- U193 pad 1: Net-(D95-A) -> Net-(D127-A)
- U193 pad 2: Net-(D159-A) -> Net-(D175-A)
- U193 pad 4: /D7 -> /D5
- U194 pad 1: Net-(D96-A) -> /D6
- U194 pad 2: Net-(D160-A) -> Net-(D112-A)
- U194 pad 4: /D7 -> Net-(D176-A)
- U195 pad 1: Net-(D97-A) -> /D6
- U195 pad 2: Net-(D161-A) -> Net-(D113-A)
- U195 pad 4: /D7 -> Net-(D177-A)
- U196 pad 1: Net-(D98-A) -> /D6
- U196 pad 2: Net-(D162-A) -> Net-(D114-A)
- U196 pad 4: /D7 -> Net-(D178-A)
- U197 pad 1: Net-(D99-A) -> /D6
- U197 pad 2: Net-(D163-A) -> Net-(D115-A)
- U197 pad 4: /D7 -> Net-(D179-A)
- U2 pad 4: Net-(D24-A) -> /Address Decoder/nA1
- U20 pad 1: (no net) -> /Address Decoder/nA4
- U20 pad 2: /Column Select/A7 -> /Address Decoder/nA3
- U20 pad 4: Net-(D42-A) -> /Address Decoder/HA0
- U21 pad 1: (no net) -> /Address Decoder/nA4
- U21 pad 2: /Column Select/A8 -> /Address Decoder/A3
- U21 pad 4: Net-(D43-A) -> /Address Decoder/HA1
- U22 pad 1: (no net) -> /Address Decoder/A4
- U22 pad 2: /Column Select/A9 -> /Address Decoder/nA3
- U22 pad 4: Net-(D44-A) -> /Address Decoder/HA2
- U23 pad 1: (no net) -> /Address Decoder/A4
- U23 pad 2: /Column Select/A10 -> /Address Decoder/A3
- U23 pad 4: Net-(D45-A) -> /Address Decoder/HA3
- U24 pad 1: Net-(D43-A) -> /Address Decoder/nA6
- U24 pad 2: Net-(D42-A) -> /Address Decoder/nA5
- U24 pad 4: /Column Select/GA0 -> /Address Decoder/HB0
- U25 pad 1: Net-(D43-A) -> /Address Decoder/nA6
- U25 pad 2: /Column Select/A7 -> /Address Decoder/A5
- U25 pad 4: /Column Select/GA1 -> /Address Decoder/HB1
- U26 pad 1: /Column Select/A8 -> /Address Decoder/A6
- U26 pad 2: Net-(D42-A) -> /Address Decoder/nA5
- U26 pad 4: /Column Select/GA2 -> /Address Decoder/HB2
- U27 pad 1: /Column Select/A8 -> /Address Decoder/A6
- U27 pad 2: /Column Select/A7 -> /Address Decoder/A5
- U27 pad 4: /Column Select/GA3 -> /Address Decoder/HB3
- U28 pad 1: Net-(D45-A) -> /Address Decoder/HB0
- U28 pad 2: Net-(D44-A) -> /Address Decoder/HA0
- U28 pad 4: /Column Select/GB0 -> /Address Decoder/DEC4_0
- U29 pad 1: Net-(D45-A) -> /Address Decoder/HB0
- U29 pad 2: /Column Select/A9 -> /Address Decoder/HA1
- U29 pad 4: /Column Select/GB1 -> /DEC4_1
- U3 pad 4: Net-(D25-A) -> /Address Decoder/nA2
- U30 pad 1: /Column Select/A10 -> /Address Decoder/HB0
- U30 pad 2: Net-(D44-A) -> /Address Decoder/HA2
- U30 pad 4: /Column Select/GB2 -> /DEC4_2
- U31 pad 1: /Column Select/A10 -> /Address Decoder/HB0
- U31 pad 2: /Column Select/A9 -> /Address Decoder/HA3
- U31 pad 4: /Column Select/GB3 -> /DEC4_3
- U32 pad 1: /Column Select/GB0 -> /Address Decoder/HB1
- U32 pad 2: /Column Select/GA0 -> /Address Decoder/HA0
- U32 pad 4: /COL_SEL_0 -> /DEC4_4
- U33 pad 1: /Column Select/GB0 -> /Address Decoder/HB1
- U33 pad 2: /Column Select/GA1 -> /Address Decoder/HA1
- U33 pad 4: /COL_SEL_1 -> /DEC4_5
- U34 pad 1: /Column Select/GB0 -> /Address Decoder/HB1
- U34 pad 2: /Column Select/GA2 -> /Address Decoder/HA2
- U34 pad 4: /COL_SEL_2 -> /DEC4_6
- U35 pad 1: /Column Select/GB0 -> /Address Decoder/HB1
- U35 pad 2: /Column Select/GA3 -> /Address Decoder/HA3
- U35 pad 4: /COL_SEL_3 -> /DEC4_7
- U36 pad 1: /Column Select/GB1 -> /Address Decoder/HB2
- U36 pad 2: /Column Select/GA0 -> /Address Decoder/HA0
- U36 pad 4: /COL_SEL_4 -> /DEC4_8
- U37 pad 1: /Column Select/GB1 -> /Address Decoder/HB2
- U37 pad 2: /Column Select/GA1 -> /Address Decoder/HA1
- U37 pad 4: /COL_SEL_5 -> /DEC4_9
- U38 pad 1: /Column Select/GB1 -> /Address Decoder/HB2
- U38 pad 2: /Column Select/GA2 -> /Address Decoder/HA2
- U38 pad 4: /COL_SEL_6 -> /DEC4_10
- U39 pad 1: /Column Select/GB1 -> /Address Decoder/HB2
- U39 pad 2: /Column Select/GA3 -> /Address Decoder/HA3
- U39 pad 4: /COL_SEL_7 -> /DEC4_11
- U4 pad 4: Net-(D26-A) -> /Address Decoder/nA3
- U40 pad 1: /Column Select/GB2 -> /Address Decoder/HB3
- U40 pad 2: /Column Select/GA0 -> /Address Decoder/HA0
- U40 pad 4: /COL_SEL_8 -> /DEC4_12
- U41 pad 1: /Column Select/GB2 -> /Address Decoder/HB3
- U41 pad 2: /Column Select/GA1 -> /Address Decoder/HA1
- U41 pad 4: /COL_SEL_9 -> /DEC4_13
- U42 pad 1: /Column Select/GB2 -> /Address Decoder/HB3
- U42 pad 2: /Column Select/GA2 -> /Address Decoder/HA2
- U42 pad 4: /COL_SEL_10 -> /DEC4_14
- U43 pad 1: /Column Select/GB2 -> /Address Decoder/HB3
- U43 pad 2: /Column Select/GA3 -> /Address Decoder/HA3
- U43 pad 4: /COL_SEL_11 -> /DEC4_15
- U44 pad 1: /Column Select/GB3 -> /Address Decoder/DEC3_0
- U44 pad 2: /Column Select/GA0 -> /Address Decoder/DEC4_0
- U44 pad 4: /COL_SEL_12 -> /Address Decoder/ROW_SEL_0
- U45 pad 1: /Column Select/GB3 -> /Address Decoder/DEC3_1
- U45 pad 2: /Column Select/GA1 -> /Address Decoder/DEC4_0
- U45 pad 4: /COL_SEL_13 -> /Address Decoder/ROW_SEL_1
- U46 pad 1: /Column Select/GB3 -> /Address Decoder/DEC3_2
- U46 pad 2: /Column Select/GA2 -> /Address Decoder/DEC4_0
- U46 pad 4: /COL_SEL_14 -> /Address Decoder/ROW_SEL_2
- U47 pad 1: /Column Select/GB3 -> /Address Decoder/DEC3_3
- U47 pad 2: /Column Select/GA3 -> /Address Decoder/DEC4_0
- U47 pad 4: /COL_SEL_15 -> /Address Decoder/ROW_SEL_3
- U48 pad 2: /Control Logic/nCE -> /Column Select/A7
- U49 pad 2: /Control Logic/nOE -> /Column Select/A8
- U5 pad 4: Net-(D27-A) -> /Address Decoder/nA4
- U50 pad 2: /Control Logic/nWE -> /Column Select/A9
- U51 pad 1: Net-(D70-A) -> (no net)
- U51 pad 2: Net-(D72-A) -> /Column Select/A10
- U51 pad 4: /WRITE_ACTIVE -> Net-(D73-A)
- U52 pad 1: Net-(D70-A) -> Net-(D71-A)
- U52 pad 2: Net-(D71-A) -> Net-(D70-A)
- U52 pad 4: Net-(D73-A) -> /Column Select/GA0
- U53 pad 1: Net-(D73-A) -> Net-(D71-A)
- U53 pad 2: /Control Logic/nWE -> /Column Select/A7
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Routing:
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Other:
- board size 200 x 84 mm -> 221 x 106 mm
- board text added: "DEC3"
- board text added: "DEC4"
- board text removed: "PROBE"

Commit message: Fix a bunch of issues
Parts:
- J3: value PinHeader_1x16_P2.54mm_Vertical -> PinHeader_1x14_P2.54mm_Vertical; footprint Connector_PinHeader_2.54mm:PinHeader_1x16_P2.54mm_Vertical -> Connector_PinHeader_2.54mm:PinHeader_1x14_P2.54mm_Vertical
- J4: value PinHeader_1x14_P2.54mm_Vertical -> PinHeader_1x16_P2.54mm_Vertical; footprint Connector_PinHeader_2.54mm:PinHeader_1x14_P2.54mm_Vertical -> Connector_PinHeader_2.54mm:PinHeader_1x16_P2.54mm_Vertical
- moved J2 123.0 mm to (141.0, 27.8), turned to 90 degrees
- moved J4 101.8 mm to (97.9, 27.8)
- moved D70 6.00 mm to (133.3, 95.2)
- moved D75 6.00 mm to (128.3, 91.2)
- moved D76 6.00 mm to (133.3, 91.2)
- moved D87 6.00 mm to (128.3, 87.2)
- moved D88 6.00 mm to (133.3, 87.2)
- moved R70 6.00 mm to (133.3, 95.2)
- moved R75 6.00 mm to (128.3, 91.2)
- moved R76 6.00 mm to (133.3, 91.2)
- moved R87 6.00 mm to (128.3, 87.2)
- moved R88 6.00 mm to (133.3, 87.2)
- moved D100 6.00 mm to (89.4, 54.2)
- moved D101 6.00 mm to (89.4, 62.8)
- moved D102 6.00 mm to (89.4, 41.2)
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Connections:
- D23 pad 2: /Address Decoder/nA0 -> /Address Decoder/nA6
- D24 pad 2: /Address Decoder/nA1 -> /Address Decoder/nA5
- D25 pad 2: /Address Decoder/nA2 -> /Address Decoder/nA4
- D27 pad 2: /Address Decoder/nA4 -> /Address Decoder/nA2
- D28 pad 2: /Address Decoder/nA5 -> /Address Decoder/nA1
- D29 pad 2: /Address Decoder/nA6 -> /Address Decoder/nA0
- J3 pad 1: /DEC4_1 -> /COL_SEL_2
- J3 pad 10: /DEC4_10 -> /COL_SEL_11
- J3 pad 11: /DEC4_11 -> /COL_SEL_12
- J3 pad 12: /DEC4_12 -> /COL_SEL_13
- J3 pad 13: /DEC4_13 -> /COL_SEL_14
- J3 pad 14: /DEC4_14 -> /COL_SEL_15
- J3 pad 2: /DEC4_2 -> /COL_SEL_3
- J3 pad 3: /DEC4_3 -> /COL_SEL_4
- J3 pad 4: /DEC4_4 -> /COL_SEL_5
- J3 pad 5: /DEC4_5 -> /COL_SEL_6
- J3 pad 6: /DEC4_6 -> /COL_SEL_7
- J3 pad 7: /DEC4_7 -> /COL_SEL_8
- J3 pad 8: /DEC4_8 -> /COL_SEL_9
- J3 pad 9: /DEC4_9 -> /COL_SEL_10
- J4 pad 1: /COL_SEL_2 -> /DEC4_1
- J4 pad 10: /COL_SEL_11 -> /DEC4_10
- J4 pad 11: /COL_SEL_12 -> /DEC4_11
- J4 pad 12: /COL_SEL_13 -> /DEC4_12
- J4 pad 13: /COL_SEL_14 -> /DEC4_13
- J4 pad 14: /COL_SEL_15 -> /DEC4_14
- J4 pad 2: /COL_SEL_3 -> /DEC4_2
- J4 pad 3: /COL_SEL_4 -> /DEC4_3
- J4 pad 4: /COL_SEL_5 -> /DEC4_4
- J4 pad 5: /COL_SEL_6 -> /DEC4_5
- J4 pad 6: /COL_SEL_7 -> /DEC4_6
- J4 pad 7: /COL_SEL_8 -> /DEC4_7
- J4 pad 8: /COL_SEL_9 -> /DEC4_8
- J4 pad 9: /COL_SEL_10 -> /DEC4_9
- U1 pad 2: /Address Decoder/A0 -> /Address Decoder/A6
- U1 pad 4: /Address Decoder/nA0 -> /Address Decoder/nA6
- U2 pad 2: /Address Decoder/A1 -> /Address Decoder/A5
- U2 pad 4: /Address Decoder/nA1 -> /Address Decoder/nA5
- U3 pad 2: /Address Decoder/A2 -> /Address Decoder/A4
- U3 pad 4: /Address Decoder/nA2 -> /Address Decoder/nA4
- U5 pad 2: /Address Decoder/A4 -> /Address Decoder/A2
- U5 pad 4: /Address Decoder/nA4 -> /Address Decoder/nA2
- U6 pad 2: /Address Decoder/A5 -> /Address Decoder/A1
- U6 pad 4: /Address Decoder/nA5 -> /Address Decoder/nA1
- U7 pad 2: /Address Decoder/A6 -> /Address Decoder/A0
- U7 pad 4: /Address Decoder/nA6 -> /Address Decoder/nA0
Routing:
- added copper zone on In1.Cu, net GND
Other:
- board size 221 x 106 mm -> 227 x 91 mm

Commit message: Fix more issues
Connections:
- D10 pad 2: /D5 -> /nCE
- D11 pad 2: /D4 -> /D7
- D12 pad 2: /D3 -> /D6
- D13 pad 2: /D2 -> /D5
- D14 pad 2: /D1 -> /D4
- D15 pad 2: /D0 -> /D3
- D16 pad 2: /nOE -> /D2
- D17 pad 2: /nWE -> /D1
- D18 pad 2: /nCE -> /D0
- D8 pad 2: /D7 -> /nOE
- D9 pad 2: /D6 -> /nWE
- J1 pad 10: /D1 -> /D4
- J1 pad 11: /D2 -> /D5
- J1 pad 12: /D3 -> /D6
- J1 pad 13: /D4 -> /D7
- J1 pad 14: /D5 -> /nCE
- J1 pad 15: /D6 -> /nWE
- J1 pad 16: /D7 -> /nOE
- J1 pad 6: /nCE -> /D0
- J1 pad 7: /nWE -> /D1
- J1 pad 8: /nOE -> /D2
- J1 pad 9: /D0 -> /D3
